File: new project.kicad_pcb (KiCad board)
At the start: 2 copper layers, 1 part

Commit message: Wiring Done
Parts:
- removed REF**: ATPAK-2, Package_TO_SOT_SMD:ATPAK-2
- added J1: LED 0.170amps, Connector_Molex:Molex_Micro-Fit_3.0_43650-0200_1x02_P3.00mm_Horizontal, F.Cu at (115.5, 67.4)
- added J2: Tractive Battery, Resistor_SMD:R_0201_0603Metric, F.Cu at (122.1, 69.2)
- added R1: 1800, Capacitor_SMD:C_0603_1608Metric, F.Cu at (125.8, 69.2)
- added U1: ~, Package_TO_SOT_SMD:TO-252-2, F.Cu at (130.9, 63.7)
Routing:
- net Net-(J1-Pin_2): track 0.00 -> 23.2 mm
- net GND: track 0.00 -> 12.6 mm
- net Net-(U1-Cathode): track 0.00 -> 3.48 mm
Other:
- board outline added: 33.8 x 23 mm

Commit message: everything works type
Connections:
- J1 pad 1: unconnected-(J1-Pin_1-Pad1) -> +4V
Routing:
- net +4V: track 0.00 -> 7.02 mm
- net GND: track 12.6 -> 11.8 mm
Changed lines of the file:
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@@
 	)
 	(net 0 "")
-	(net 1 "unconnected-(J1-Pin_1-Pad1)")
-	(net 2 "Net-(J1-Pin_2)")
-	(net 3 "GND")
-	(net 4 "+4V")
-	(net 5 "Net-(U1-Cathode)")
+	(net 1 "Net-(J1-Pin_2)")
+	(net 2 "GND")
+	(net 3 "+4V")
+	(net 4 "Net-(U1-Cathode)")
 	(footprint "Resistor_SMD:R_0201_0603Metric"
 		(layer "F.Cu")
@@
 		(tags "resistor")
 		(property "Reference" "J2"
-			(at 0 -1.05 0)
+			(at 0.12422 -1.45992 0)
 			(layer "F.SilkS")
 			(effects
@@
 			(layers "F.Cu" "F.Mask")
 			(roundrect_rratio 0.25)
-			(net 4 "+4V")
+			(net 3 "+4V")
 			(pinfunction "Pin_1")
 			(pintype "passive")
@@
 			(layers "F.Cu" "F.Mask")
 			(roundrect_rratio 0.25)
-			(net 3 "GND")
+			(net 2 "GND")
 			(pinfunction "Pin_2")
 			(pintype "passive")
@@
 			(layers "F.Cu" "F.Mask" "F.Paste")
 			(roundrect_rratio 0.25)
-			(net 3 "GND")
+			(net 2 "GND")
 			(pintype "passive")
 		)
@@
 			(layers "F.Cu" "F.Mask" "F.Paste")
 			(roundrect_rratio 0.25)
-			(net 5 "Net-(U1-Cathode)")
+			(net 4 "Net-(U1-Cathode)")
 			(pintype "passive")
 		)
@@
 			(layers "F.Cu" "F.Mask" "F.Paste")
 			(roundrect_rratio 0.208333)
-			(net 3 "GND")
+			(net 2 "GND")
 			(pinfunction "Gate")
 			(pintype "input")
@@
 			(layers "F.Cu" "F.Mask")
 			(roundrect_rratio 0.043103)
-			(net 2 "Net-(J1-Pin_2)")
+			(net 1 "Net-(J1-Pin_2)")
 			(pinfunction "Anode")
 			(pintype "input")
@@
 			(layers "F.Cu" "F.Mask" "F.Paste")
 			(roundrect_rratio 0.208333)
-			(net 5 "Net-(U1-Cathode)")
+			(net 4 "Net-(U1-Cathode)")
 			(pinfunction "Cathode")
 			(pintype "input")
@@
 		(tags "connector Molex Micro-Fit_3.0 horizontal")
 		(property "Reference" "J1"
-			(at 16.76284 -10.19286 90)
+			(at 1.90424 -10.0319 90)
 			(layer "F.SilkS")
 			(effects
@@
 			(remove_unused_layers no)
 			(roundrect_rratio 0.166667)
-			(net 1 "unconnected-(J1-Pin_1-Pad1)")
+			(net 3 "+4V")
 			(pinfunction "Pin_1")
 			(pintype "passive")
@@
 			(layers "*.Cu" "*.Mask")
 			(remove_unused_layers no)
-			(net 2 "Net-(J1-Pin_2)")
+			(net 1 "Net-(J1-Pin_2)")
 			(pinfunction "Pin_2")
 			(pintype "passive")
@@
 		(width 0.2)
 		(layer "F.Cu")
-		(net 2)
+		(net 1)
 	)
 	(segment
@@
 		(width 0.2)
 		(layer "F.Cu")
-		(net 2)
+		(net 1)
 	)
 	(segment
@@
 		(width 0.2)
 		(layer "F.Cu")
-		(net 2)
+		(net 1)
 	)
 	(segment
@@
 		(width 0.2)
 		(layer "F.Cu")
+		(net 1)
+	)
+	(segment
+		(start 123.75 63.56068)
+		(end 125.88356 61.42712)
+		(width 0.2)
+		(layer "F.Cu")
 		(net 2)
 	)
 	(segment
-		(start 124.20116 61.42712)
-		(end 125.88356 61.42712)
-		(width 0.2)
-		(layer "F.Cu")
-		(net 3)
+		(start 125.03598 69.17944)
+		(end 123.75 67.89346)
+		(width 0.2)
+		(layer "F.Cu")
+		(net 2)
+	)
+	(segment
+		(start 123.75 67.89346)
+		(end 123.75 63.56068)
+		(width 0.2)
+		(layer "F.Cu")
+		(net 2)
+	)
+	(segment
+		(start 125.0055 69.20992)
+		(end 125.03598 69.17944)
+		(width 0.2)
+		(layer "F.Cu")
+		(net 2)
 	)
 	(segment
@@
 		(width 0.2)
 		(layer "F.Cu")
+		(net 2)
+	)
+	(segment
+		(start 115.5319 67.40424)
+		(end 120.0001 67.40424)
+		(width 0.2)
+		(layer "F.Cu")
 		(net 3)
 	)
 	(segment
-		(start 124.02058 68.16404)
-		(end 124.02058 61.468)
-		(width 0.2)
-		(layer "F.Cu")
-		(net 3)
-	)
-	(segment
-		(start 125.03598 69.17944)
-		(end 124.02058 68.16404)
-		(width 0.2)
-		(layer "F.Cu")
-		(net 3)
-	)
-	(segment
-		(start 125.0055 69.20992)
-		(end 125.03598 69.17944)
-		(width 0.2)
-		(layer "F.Cu")
-		(net 3)
-	)
-	(segment
-		(start 124.16028 61.468)
-		(end 124.20116 61.42712)
-		(width 0.2)
-		(layer "F.Cu")
-		(net 3)
-	)
-	(segment
-		(start 124.02058 61.468)
-		(end 124.16028 61.468)
+		(start 120.0001 67.40424)
+		(end 121.80578 69.20992)
 		(width 0.2)
 		(layer "F.Cu")
@@
 		(width 0.2)
 		(layer "F.Cu")
-		(net 5)
+		(net 4)
 	)
 	(segment
@@
 		(width 0.2)
 		(layer "F.Cu")
-		(net 5)
+		(net 4)
 	)
 	(embedded_fonts no)

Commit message: UPDATE
This should update everything now?? THINGS KEEP GETTING DELETED
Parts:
- J2: footprint Resistor_SMD:R_0201_0603Metric -> Connector_Molex:Molex_Micro-Fit_3.0_43650-0200_1x02_P3.00mm_Horizontal
- R1: value 1800 -> 18000
- moved J2 15.7 mm to (135.5, 77.4), turned to 180 degrees
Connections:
- J1 pad 1: +4V -> unconnected-(J1-Pin_1-Pad1)
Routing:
- net Net-(J1-Pin_2): track 23.2 -> 4.44 mm
- net GND: track 11.8 -> 0.04 mm
- net +4V: track 7.02 -> 0.00 mm
- net Net-(U1-Cathode): track 3.48 -> 0.00 mm
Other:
- board size 33.8 x 23 mm -> 44.9 x 35 mm

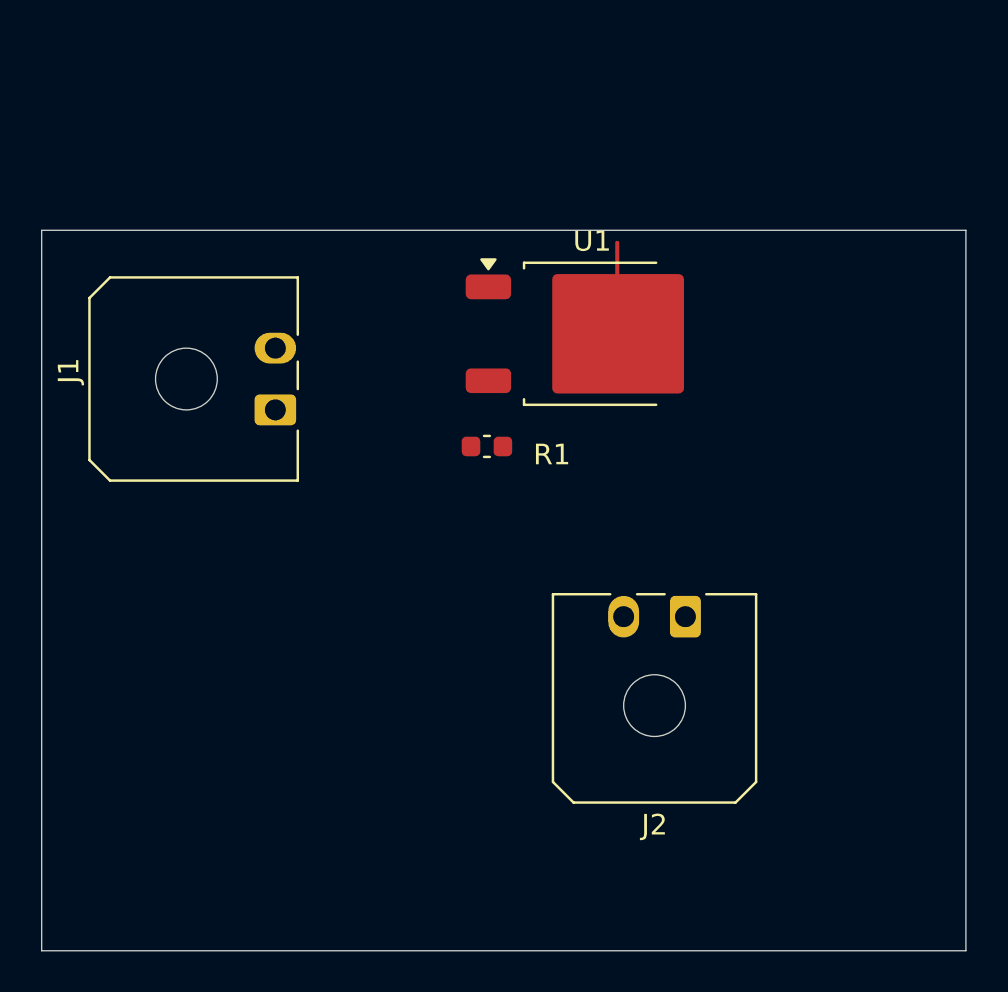
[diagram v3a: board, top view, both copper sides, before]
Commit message: Prototype
Some error stills, but structure is overall built
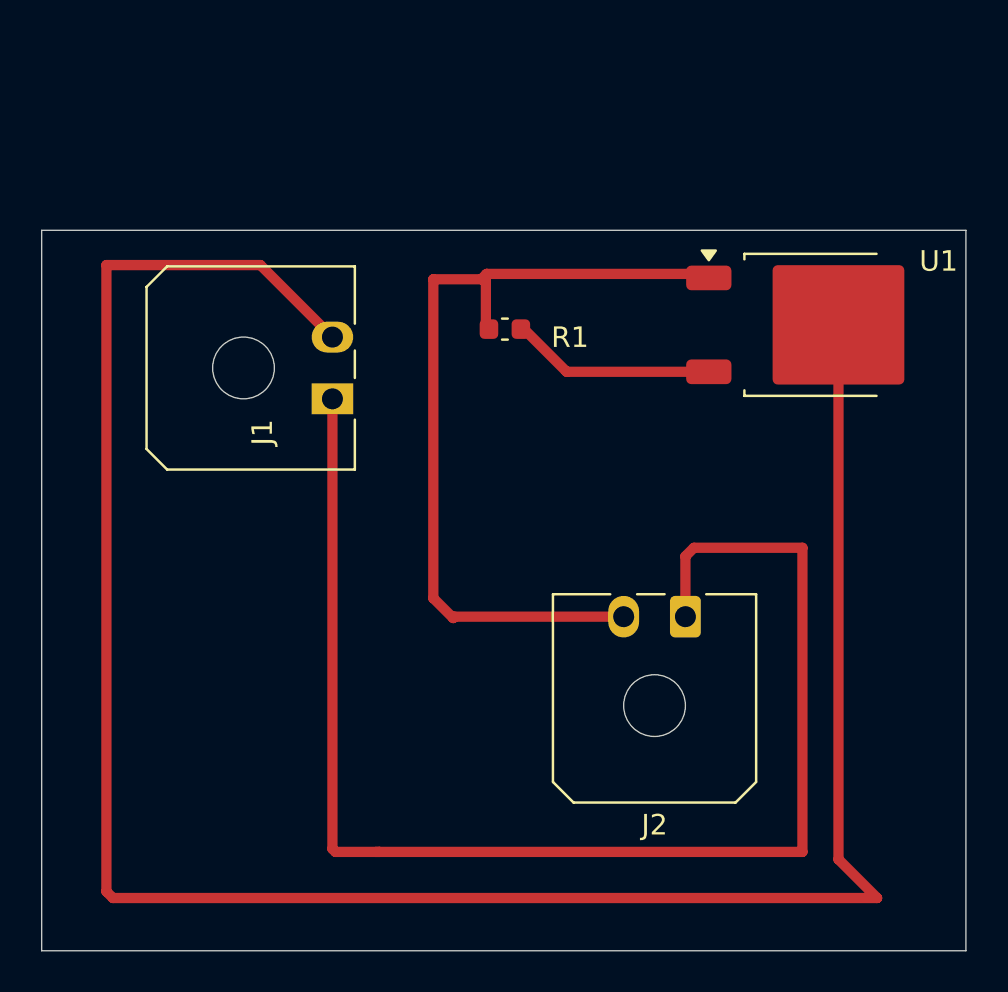
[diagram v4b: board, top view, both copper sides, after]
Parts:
- moved U1 10.7 mm to (141.6, 63.3)
- moved R1 5.77 mm to (126.7, 63.5)
- moved J1 2.82 mm to (118.3, 66.9)
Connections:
- J1 pad 1: unconnected-(J1-Pin_1-Pad1) -> +4V
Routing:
- net Net-(J1-Pin_2): track 4.44 -> 109.1 mm
- net +4V: track 0.00 -> 68.5 mm
- net GND: track 0.04 -> 41.5 mm
- net Net-(U1-Cathode): track 0.00 -> 9.99 mm
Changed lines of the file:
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@@
 	(net 3 "+4V")
 	(net 4 "Net-(U1-Cathode)")
-	(net 5 "unconnected-(J1-Pin_1-Pad1)")
 	(footprint "Connector_Molex:Molex_Micro-Fit_3.0_43650-0200_1x02_P3.00mm_Horizontal"
 		(layer "F.Cu")
@@
 	(footprint "Capacitor_SMD:C_0603_1608Metric"
 		(layer "F.Cu")
-		(at 125.81098 69.17944)
+		(at 126.68474 63.47968)
 		(descr "Capacitor SMD 0603 (1608 Metric), square (rectangular) end terminal, IPC-7351 nominal, (Body size source: IPC-SM-782 page 76, https://www.pcb-3d.com/wordpress/wp-content/uploads/ipc-sm-782a_amendment_1_and_2.pdf), generated with kicad-footprint-generator")
 		(tags "capacitor")
@@
 		)
 		(fp_text user "${REFERENCE}"
-			(at 0 0 0)
+			(at 1.71734 -1.80848 0)
 			(layer "F.Fab")
 			(effects
@@
 	(footprint "Package_TO_SOT_SMD:TO-252-2"
 		(layer "F.Cu")
-		(at 130.92356 63.70712)
+		(at 141.6291 63.27294)
 		(descr "TO-252/DPAK SMD package, http://www.infineon.com/cms/en/product/packages/PG-TO252/PG-TO252-3-1/")
 		(tags "DPAK TO-252 DPAK-3 TO-252-3 SOT-428")
 		(property "Reference" "U1"
-			(at 0 -4.5 0)
+			(at 6.12016 -3.09272 0)
 			(layer "F.SilkS")
 			(effects
@@
 	(footprint "Connector_Molex:Molex_Micro-Fit_3.0_43650-0200_1x02_P3.00mm_Horizontal"
 		(layer "F.Cu")
-		(at 115.5319 67.40424 90)
+		(at 118.30504 66.8669 90)
 		(descr "Molex Micro-Fit 3.0 Connector System, 43650-0200 (compatible alternatives: 43650-0201, 43650-0202), 2 Pins per row (https://www.molex.com/pdm_docs/sd/436500300_sd.pdf), generated with kicad-footprint-generator")
 		(tags "connector Molex Micro-Fit_3.0 horizontal")
 		(property "Reference" "J1"
-			(at 1.90424 -10.0319 90)
+			(at -1.62928 -3.40306 90)
 			(layer "F.SilkS")
 			(effects
@@
 			(layers "*.Cu" "*.Mask")
 		)
-		(pad "1" thru_hole roundrect
+		(pad "1" thru_hole rect
 			(at 0 0 90)
 			(size 1.5 2.02)
@@
 			(layers "*.Cu" "*.Mask")
 			(remove_unused_layers no)
-			(roundrect_rratio 0.166667)
-			(net 5 "unconnected-(J1-Pin_1-Pad1)")
+			(net 3 "+4V")
 			(pinfunction "Pin_1")
 			(pintype "passive")
@@
 	)
 	(segment
-		(start 132.18356 63.70712)
-		(end 132.1435 63.66706)
+		(start 142.8891 63.27294)
+		(end 142.84904 63.23288)
 		(width 0.2)
 		(layer "F.Cu")
@@
 	)
 	(segment
-		(start 132.1435 63.66706)
-		(end 132.1435 59.28868)
+		(start 107.64266 91.11742)
+		(end 144.7673 91.11742)
+		(width 0.5)
+		(layer "F.Cu")
+		(net 1)
+	)
+	(segment
+		(start 118.30504 63.8669)
+		(end 114.80632 60.36818)
+		(width 0.5)
+		(layer "F.Cu")
+		(net 1)
+	)
+	(segment
+		(start 144.7673 91.11742)
+		(end 142.8891 89.23922)
+		(width 0.5)
+		(layer "F.Cu")
+		(net 1)
+	)
+	(segment
+		(start 114.80632 60.36818)
+		(end 107.32516 60.36818)
+		(width 0.5)
+		(layer "F.Cu")
+		(net 1)
+	)
+	(segment
+		(start 142.8891 89.23922)
+		(end 142.8891 63.27294)
+		(width 0.5)
+		(layer "F.Cu")
+		(net 1)
+	)
+	(segment
+		(start 107.32516 60.36818)
+		(end 107.32516 90.79992)
+		(width 0.5)
+		(layer "F.Cu")
+		(net 1)
+	)
+	(segment
+		(start 107.32516 90.79992)
+		(end 107.64266 91.11742)
+		(width 0.5)
+		(layer "F.Cu")
+		(net 1)
+	)
+	(segment
+		(start 125.80112 60.79744)
+		(end 125.75874 60.83982)
+		(width 0.5)
+		(layer "F.Cu")
+		(net 2)
+	)
+	(segment
+		(start 136.3936 60.79744)
+		(end 125.80112 60.79744)
+		(width 0.5)
+		(layer "F.Cu")
+		(net 2)
+	)
+	(segment
+		(start 125.75874 60.83982)
+		(end 125.75874 63.47968)
+		(width 0.5)
+		(layer "F.Cu")
+		(net 2)
+	)
+	(segment
+		(start 123.20524 61.05906)
+		(end 125.5395 61.05906)
+		(width 0.5)
+		(layer "F.Cu")
+		(net 2)
+	)
+	(segment
+		(start 136.5891 60.99294)
+		(end 136.3936 60.79744)
+		(width 0.5)
+		(layer "F.Cu")
+		(net 2)
+	)
+	(segment
+		(start 124.24156 77.44968)
+		(end 124.17298 77.51826)
+		(width 0.5)
+		(layer "F.Cu")
+		(net 2)
+	)
+	(segment
+		(start 132.45338 77.44968)
+		(end 124.24156 77.44968)
+		(width 0.5)
+		(layer "F.Cu")
+		(net 2)
+	)
+	(segment
+		(start 124.17298 77.51826)
+		(end 123.20524 76.55052)
+		(width 0.5)
+		(layer "F.Cu")
+		(net 2)
+	)
+	(segment
+		(start 125.87926 63.51016)
+		(end 125.90974 63.47968)
 		(width 0.2)
 		(layer "F.Cu")
-		(net 1)
-	)
-	(segment
-		(start 125.0055 69.20992)
-		(end 125.03598 69.17944)
-		(width 0.2)
-		(layer "F.Cu")
 		(net 2)
 	)
+	(segment
+		(start 123.20524 76.55052)
+		(end 123.20524 61.05906)
+		(width 0.5)
+		(layer "F.Cu")
+		(net 2)
+	)
+	(segment
+		(start 125.5395 61.05906)
+		(end 125.80112 60.79744)
+		(width 0.5)
+		(layer "F.Cu")
+		(net 2)
+	)
+	(segment
+		(start 135.86714 74.10196)
+		(end 135.45338 74.51572)
+		(width 0.5)
+		(layer "F.Cu")
+		(net 3)
+	)
+	(segment
+		(start 120.59412 88.87714)
+		(end 141.1381 88.87714)
+		(width 0.5)
+		(layer "F.Cu")
+		(net 3)
+	)
+	(segment
+		(start 120.59412 88.87714)
+		(end 118.4529 88.87714)
+		(width 0.5)
+		(layer "F.Cu")
+		(net 3)
+	)
+	(segment
+		(start 118.4529 88.87714)
+		(end 118.30504 88.72928)
+		(width 0.5)
+		(layer "F.Cu")
+		(net 3)
+	)
+	(segment
+		(start 135.45338 74.51572)
+		(end 135.45338 77.44968)
+		(width 0.5)
+		(layer "F.Cu")
+		(net 3)
+	)
+	(segment
+		(start 141.1381 88.87714)
+		(end 141.1381 74.10196)
+		(width 0.5)
+		(layer "F.Cu")
+		(net 3)
+	)
+	(segment
+		(start 141.1381 74.10196)
+		(end 135.86714 74.10196)
+		(width 0.5)
+		(layer "F.Cu")
+		(net 3)
+	)
+	(segment
+		(start 118.30504 88.72928)
+		(end 118.30504 66.8669)
+		(width 0.5)
+		(layer "F.Cu")
+		(net 3)
+	)
+	(segment
+		(start 120.40616 88.87714)
+		(end 120.59412 88.87714)
+		(width 0.5)
+		(layer "F.Cu")
+		(net 3)
+	)
+	(segment
+		(start 136.5891 65.55294)
+		(end 129.684 65.55294)
+		(width 0.5)
+		(layer "F.Cu")
+		(net 4)
+	)
+	(segment
+		(start 129.684 65.55294)
+		(end 127.61074 63.47968)
+		(width 0.5)
+		(layer "F.Cu")
+		(net 4)
+	)
+	(segment
+		(start 127.61074 63.63068)
+		(end 127.61074 63.47968)
+		(width 0.5)
+		(layer "F.Cu")
+		(net 4)
+	)
 	(embedded_fonts no)
